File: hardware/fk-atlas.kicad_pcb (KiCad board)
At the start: 4 copper layers, 88.4 x 80.3 mm, 162 parts, among them J1 CONN_02x05_SWD, J10 CONN_01x04, J2 MICRO-USB-VERT-TOP, J201 CONN_01X02, J3 CONN_01x02, J301 CONN_01X02, J4 CONN_01x03_SERIAL, J401 CONN_01X02, J5 CONN_01x05, J501 CONN_01X02, J6 CONN_01x04, J601 CONN_01X02, J7 CONN_01x05, J8 CONN_01x02, J9 MICRO-USB-HORIZ-BOTTOM, M1 MOUNT_HOLE, M2 MOUNT_HOLE, M3 MOUNT_HOLE, M4 MOUNT_HOLE, M5 FIDUCIAL, M6 FIDUCIAL, M7 FIDUCIAL, P2 ATLAS_EC_PROBE, P3 ATLAS_RTD_PROBE, P4 ATLAS_PH_PROBE, P5 ATLAS_DO_PROBE, P6 ATLAS_ORP_PROBE, Q4 2N7002LT1G, SW1 SPNO, U1 S25FL116K0XMFI041, U2 ATSAMD21G18A-AU, U201 ADM3260, U202 ATLAS_EC, U3 MCP1700T-3302E/MB, U301 ADM3260, U302 ATLAS_RTD, U4 TPS2052B, U401 ADM3260, U402 ATLAS_PH, U5 SK6812, U501 ADM3260, U502 ATLAS_DO, U601 ADM3260, U602 ATLAS_ORP, Y1 FC-135

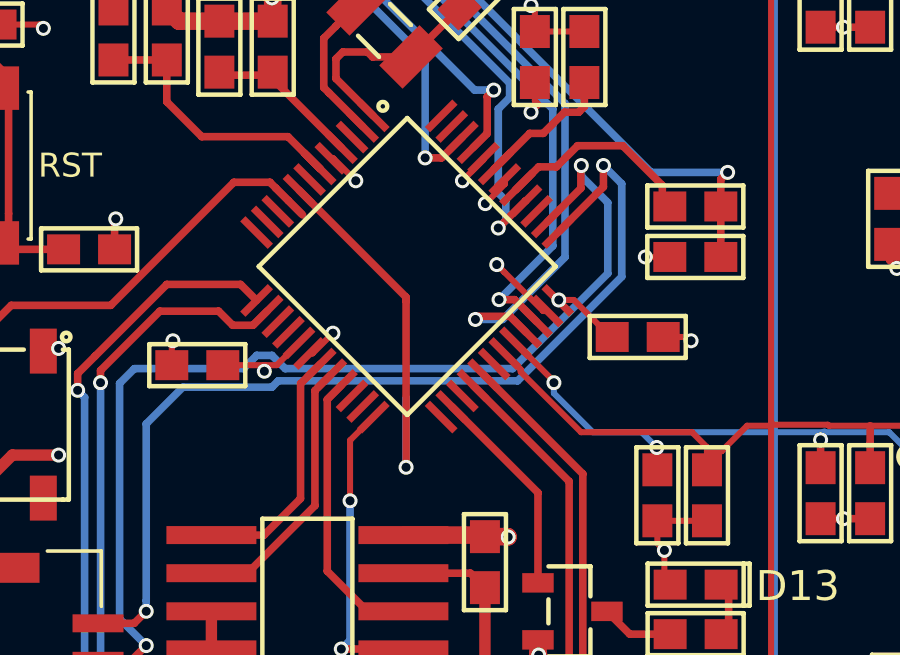
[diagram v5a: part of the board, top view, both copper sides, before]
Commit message: Cleaned up old gerber files and regenerated panelized gerbers and original file after fab found an unconnected track (A2, wasn't used for anything)
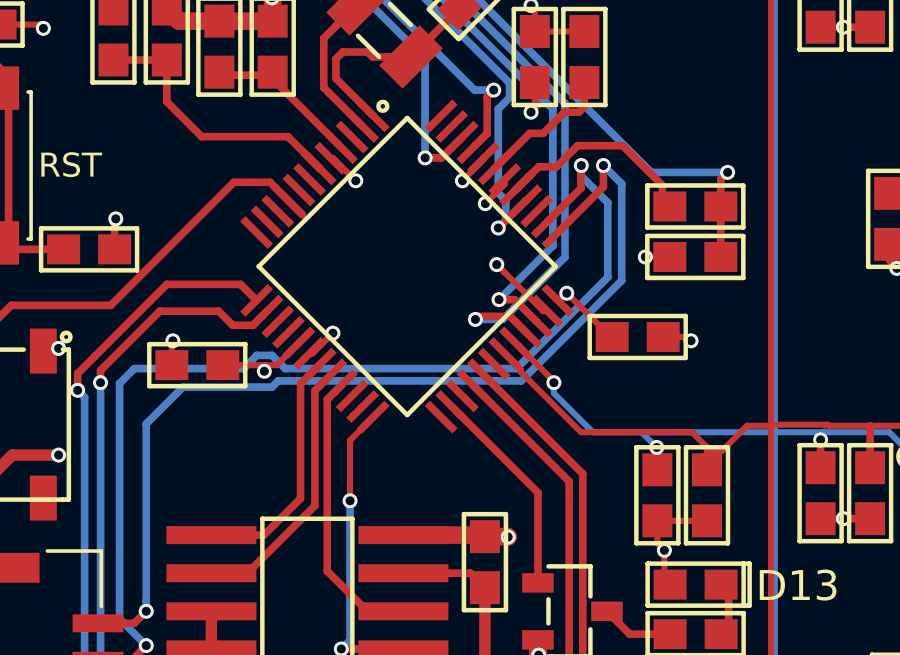
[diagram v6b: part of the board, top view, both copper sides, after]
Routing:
- net /A2: track 13.1 -> 0.00 mm, vias 1 -> 0
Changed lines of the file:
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@@
     (thickness 1.6)
     (drawings 27)
-    (tracks 1481)
+    (tracks 1475)
     (zones 0)
     (modules 162)
@@
   (segment (start 136.652 90.976661) (end 135.876745 91.751916) (width 0.254) (layer F.Cu) (net 66))
   (segment (start 135.876745 91.751916) (end 136.442661 91.186) (width 0.254) (layer F.Cu) (net 66))
-  (segment (start 132.2324 98.63834) (end 132.2324 100.9904) (width 0.254) (layer B.Cu) (net 69))
-  (segment (start 132.2324 95.452417) (end 132.2324 100.9904) (width 0.254) (layer F.Cu) (net 69))
-  (via (at 132.2324 100.9904) (size 0.5) (drill 0.3) (layers F.Cu B.Cu) (net 69))
-  (segment (start 128.664255 91.751916) (end 132.2324 95.320061) (width 0.254) (layer F.Cu) (net 69))
-  (segment (start 132.2324 95.320061) (end 132.2324 95.452417) (width 0.254) (layer F.Cu) (net 69))
   (segment (start 128.7145 98.207053) (end 129.371362 97.550191) (width 0.254) (layer F.Cu) (net 74))
   (segment (start 128.7145 102.0336) (end 128.7145 98.207053) (width 0.254) (layer F.Cu) (net 74))
@@
   (segment (start 138.811 91.646087) (end 138.811 90.932) (width 0.254) (layer F.Cu) (net 83))
   (via (at 138.811 90.932) (size 0.5) (drill 0.3) (layers F.Cu B.Cu) (net 83))
-  (segment (start 123.571 105.437447) (end 123.571 105.791) (width 0.254) (layer B.Cu) (net 83))
-  (segment (start 123.571 99.5426) (end 123.571 105.437447) (width 0.254) (layer B.Cu) (net 83))
-  (segment (start 139.4206 91.5416) (end 139.4206 94.6404) (width 0.254) (layer B.Cu) (net 83))
   (segment (start 138.811 90.932) (end 139.4206 91.5416) (width 0.254) (layer B.Cu) (net 83))
-  (segment (start 139.4206 94.6404) (end 135.95206 98.10894) (width 0.254) (layer B.Cu) (net 83))
-  (segment (start 135.95206 98.10894) (end 127.972574 98.10894) (width 0.254) (layer B.Cu) (net 83))
-  (segment (start 127.972574 98.10894) (end 127.762113 98.319401) (width 0.254) (layer B.Cu) (net 83))
   (segment (start 124.794199 98.319401) (end 123.571 99.5426) (width 0.254) (layer B.Cu) (net 83))
   (segment (start 127.762113 98.319401) (end 124.794199 98.319401) (width 0.254) (layer B.Cu) (net 83))
+  (segment (start 139.4206 94.767665) (end 136.079325 98.10894) (width 0.254) (layer B.Cu) (net 83))
+  (segment (start 123.571 105.437447) (end 123.571 105.791) (width 0.254) (layer B.Cu) (net 83))
+  (segment (start 123.571 99.5426) (end 123.571 105.437447) (width 0.254) (layer B.Cu) (net 83))
+  (segment (start 127.972574 98.10894) (end 127.762113 98.319401) (width 0.254) (layer B.Cu) (net 83))
+  (segment (start 136.079325 98.10894) (end 127.972574 98.10894) (width 0.254) (layer B.Cu) (net 83))
+  (segment (start 139.4206 91.5416) (end 139.4206 94.767665) (width 0.254) (layer B.Cu) (net 83))
   (segment (start 121.965 107.442) (end 123.063 107.442) (width 0.254) (layer F.Cu) (net 84))
   (segment (start 123.063 107.442) (end 123.571 106.934) (width 0.254) (layer F.Cu) (net 84))
@@
   (via (at 138.0744 90.932) (size 0.5) (drill 0.3) (layers F.Cu B.Cu) (net 84))
   (segment (start 136.937405 92.812576) (end 138.059119 91.690862) (width 0.254) (layer F.Cu) (net 84))
-  (segment (start 135.78372 97.70253) (end 138.955318 94.530932) (width 0.254) (layer B.Cu) (net 84))
-  (segment (start 138.0744 91.285553) (end 138.0744 90.932) (width 0.254) (layer B.Cu) (net 84))
-  (segment (start 123.17587 97.70253) (end 126.811956 97.70253) (width 0.254) (layer B.Cu) (net 84))
   (segment (start 122.68199 106.04499) (end 122.68199 98.19641) (width 0.254) (layer B.Cu) (net 84))
-  (segment (start 127.762113 97.260599) (end 128.204044 97.70253) (width 0.254) (layer B.Cu) (net 84))
-  (segment (start 138.955318 92.166471) (end 138.0744 91.285553) (width 0.254) (layer B.Cu) (net 84))
   (segment (start 126.811956 97.70253) (end 127.253887 97.260599) (width 0.254) (layer B.Cu) (net 84))
-  (segment (start 138.955318 94.530932) (end 138.955318 92.166471) (width 0.254) (layer B.Cu) (net 84))
-  (segment (start 128.204044 97.70253) (end 135.78372 97.70253) (width 0.254) (layer B.Cu) (net 84))
-  (segment (start 127.253887 97.260599) (end 127.762113 97.260599) (width 0.254) (layer B.Cu) (net 84))
-  (segment (start 122.68199 98.19641) (end 123.17587 97.70253) (width 0.254) (layer B.Cu) (net 84))
+  (segment (start 138.955318 92.166471) (end 138.0744 91.285553) (width 0.254) (layer B.Cu) (net 84))
   (segment (start 123.571 106.934) (end 122.68199 106.04499) (width 0.254) (layer B.Cu) (net 84))
+  (segment (start 138.0744 91.285553) (end 138.0744 90.932) (width 0.254) (layer B.Cu) (net 84))
+  (segment (start 138.955318 94.658196) (end 138.955318 92.166471) (width 0.254) (layer B.Cu) (net 84))
+  (segment (start 135.910984 97.70253) (end 138.955318 94.658196) (width 0.254) (layer B.Cu) (net 84))
+  (segment (start 127.762113 97.260599) (end 128.204044 97.70253) (width 0.254) (layer B.Cu) (net 84))
+  (segment (start 128.204044 97.70253) (end 135.910984 97.70253) (width 0.254) (layer B.Cu) (net 84))
+  (segment (start 123.17587 97.70253) (end 126.811956 97.70253) (width 0.254) (layer B.Cu) (net 84))
+  (segment (start 122.68199 98.19641) (end 123.17587 97.70253) (width 0.254) (layer B.Cu) (net 84))
+  (segment (start 127.253887 97.260599) (end 127.762113 97.260599) (width 0.254) (layer B.Cu) (net 84))
   (segment (start 142.9844 106.553) (end 142.9844 105.152) (width 0.254) (layer F.Cu) (net 89))
   (segment (start 142.9844 105.152) (end 142.7344 104.902) (width 0.254) (layer F.Cu) (net 89))
@@
   (via (at 133.35 76.835) (size 0.5) (drill 0.3) (layers F.Cu B.Cu) (net 111))
   (via (at 132.08 76.835) (size 0.5) (drill 0.3) (layers F.Cu B.Cu) (net 111))
-  (segment (start 137.308679 95.428871) (end 137.323775 95.413775) (width 0.203) (layer F.Cu) (net 111))
-  (via (at 137.323775 95.413775) (size 0.5) (drill 0.3) (layers F.Cu B.Cu) (net 111))
-  (segment (start 137.290958 95.428871) (end 137.308679 95.428871) (width 0.203) (layer F.Cu) (net 111))
   (segment (start 142.262283 102.774303) (end 140.608469 102.774303) (width 0.203) (layer F.Cu) (net 111))
   (via (at 140.843 103.759) (size 0.5) (drill 0.3) (layers F.Cu B.Cu) (net 111))
@@
   (segment (start 140.843 104.7106) (end 141.0344 104.902) (width 0.203) (layer F.Cu) (net 111))
   (segment (start 140.843 103.759) (end 140.843 104.7106) (width 0.203) (layer F.Cu) (net 111))
-  (segment (start 137.677328 95.413775) (end 137.323775 95.413775) (width 0.203) (layer F.Cu) (net 111))
-  (segment (start 137.820775 95.413775) (end 137.677328 95.413775) (width 0.203) (layer F.Cu) (net 111))
-  (segment (start 139.054 96.647) (end 137.820775 95.413775) (width 0.203) (layer F.Cu) (net 111))
-  (segment (start 139.104 96.647) (end 139.054 96.647) (width 0.203) (layer F.Cu) (net 111))
   (via (at 140.9065 118.5545) (size 0.5) (drill 0.3) (layers F.Cu B.Cu) (net 111))
   (segment (start 140.97 117.475) (end 140.97 118.491) (width 0.203) (layer B.Cu) (net 111))
@@
   (segment (start 132.627 72.82) (end 132.588 72.859) (width 0.203) (layer F.Cu) (net 111))
   (segment (start 134.366 72.82) (end 132.627 72.82) (width 0.203) (layer F.Cu) (net 111))
+  (segment (start 137.529829 95.19) (end 137.59 95.19) (width 0.203) (layer F.Cu) (net 111))
+  (segment (start 137.290958 95.428871) (end 137.529829 95.19) (width 0.203) (layer F.Cu) (net 111))
+  (via (at 137.59 95.19) (size 0.5) (drill 0.3) (layers F.Cu B.Cu) (net 111))
+  (segment (start 137.597 95.19) (end 137.59 95.19) (width 0.203) (layer F.Cu) (net 111))
+  (segment (start 139.104 96.647) (end 139.054 96.647) (width 0.203) (layer F.Cu) (net 111))
+  (segment (start 139.054 96.647) (end 137.597 95.19) (width 0.203) (layer F.Cu) (net 111))
   (segment (start 130.843 104.521) (end 132.4 104.521) (width 0.254) (layer F.Cu) (net 112))
   (segment (start 131.543 104.521) (end 130.843 104.521) (width 0.254) (layer F.Cu) (net 112))
